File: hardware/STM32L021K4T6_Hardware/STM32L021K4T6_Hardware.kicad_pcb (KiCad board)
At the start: 2 copper layers, 60 x 50 mm, 27 parts, among them J1 Conn_02x07_Odd_Even, J2 INPUT, J3 POWER, J4 OUTPUT, U1 STM32L021K4Tx, U2 MCP1802x-xx02xOT, U3 MCP4801

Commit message: routage-ratnest
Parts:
- moved C10 22.9 mm to (105.0, 152.0), turned to -90 degrees
- moved C1 18.1 mm to (117.0, 149.0)
- moved R2 17.1 mm to (108.0, 136.0), turned to 90 degrees
- moved C2 15.9 mm to (102.0, 137.0)
- moved C3 15.7 mm to (102.0, 135.0)
- moved C6 15.6 mm to (102.0, 146.0), turned to -90 degrees
- moved C9 14.9 mm to (103.0, 151.9), turned to -90 degrees
- moved D1 6.96 mm to (120.0, 142.0), turned to 90 degrees
- moved J1 5.11 mm to (120.0, 133.7), turned to 180 degrees
- moved L1 5.00 mm to (102.0, 141.8), turned to -90 degrees
- moved R1 4.38 mm to (120.0, 146.0), turned to -90 degrees
- moved C4 4.23 mm to (100.0, 141.8)
- moved U3 3.27 mm to (110.5, 154.4)
- moved C5 3.00 mm to (100.0, 146.0), turned to -90 degrees
- moved D2 2.12 mm to (93.0, 131.1)
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
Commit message: sav_09_02_2024_22_45_drc_check
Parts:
- moved R1 76.2 mm to (167.0, 86.0), turned to 90 degrees
- moved J1 74.0 mm to (167.5, 77.1)
- moved U3 72.0 mm to (156.5, 98.9), turned to 180 degrees
- moved C1 71.8 mm to (162.0, 93.0), turned to -90 degrees
- moved L1 71.2 mm to (146.2, 86.0), turned to 0 degrees
- moved U1 71.1 mm to (155.0, 89.2)
- moved C10 71.1 mm to (150.0, 97.0)
- moved C2 71.1 mm to (147.0, 82.0)
- moved C3 71.1 mm to (147.0, 80.0)
- moved C7 71.1 mm to (149.0, 71.0)
- moved C8 71.1 mm to (141.0, 72.0)
- moved D2 71.1 mm to (138.0, 76.1)
- moved H1 71.1 mm to (130.0, 69.0)
- moved H2 71.1 mm to (180.0, 69.0)
- moved H3 71.1 mm to (180.0, 109.0)
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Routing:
- net NRST: track 0.00 -> 89.7 mm
- net +3.3V: track 0.00 -> 82.8 mm, vias 0 -> 2
- net USART2_RX: track 0.00 -> 39.5 mm, vias 0 -> 2
- net USART2_TX: track 0.00 -> 36.4 mm, vias 0 -> 2
- net DAC_OUT: track 0.00 -> 34.6 mm
- net +3.3VA: track 0.00 -> 29.5 mm
- net ADC_IN1: track 0.00 -> 24.5 mm, vias 0 -> 1
- net +5V: track 0.00 -> 12.3 mm
- net LED_STATUS: track 0.00 -> 12.1 mm
- net SWDCK: track 0.00 -> 11.2 mm
- net SWDIO: track 0.00 -> 11.1 mm
- net DAC_nCS: track 0.00 -> 9.23 mm
- net SPI1_SCK: track 0.00 -> 7.62 mm
- net SPI1_MOSI: track 0.00 -> 5.69 mm
- net GND: track 0.00 -> 4.78 mm
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
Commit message: drc_check_ok
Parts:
- moved C6 7.00 mm to (145.0, 89.0)
- moved C4 3.00 mm to (146.0, 92.0)
- moved C5 2.00 mm to (146.0, 94.0)
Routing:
- net NRST: track 89.7 -> 75.3 mm
- net +3.3VA: track 29.5 -> 30.1 mm

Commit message: drc check bis
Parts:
- moved C6 21.4 mm to (162.0, 76.0)
- moved L1 3.95 mm to (147.7, 89.7)
- moved D1 3.31 mm to (163.7, 89.7)
- moved R1 3.31 mm to (163.7, 85.8)
- moved J2 2.37 mm to (129.7, 88.7), turned to -90 degrees
- moved U3 1.91 mm to (155.1, 97.6)
- moved C4 1.75 mm to (147.7, 91.7)
- moved C5 1.75 mm to (147.7, 93.7)
- moved U2 0.99 mm to (146.0, 71.5)
- moved C7 0.99 mm to (149.9, 70.5)
- moved C8 0.99 mm to (141.9, 71.5)
- moved D2 0.99 mm to (138.9, 75.6)
- moved R3 0.99 mm to (138.9, 71.6)
- moved C1 0.76 mm to (161.3, 93.3)
- moved R2 0.70 mm to (153.0, 81.7)
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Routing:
- net NRST: track 75.3 -> 23.9 mm, vias 0 -> 2
- net +3.3V: track 82.8 -> 66.0 mm
- net +3.3VA: track 30.1 -> 19.9 mm
- net USART2_TX: track 36.4 -> 28.1 mm
- net LED_STATUS: track 12.1 -> 4.78 mm
- net GND: track 4.78 -> 9.15 mm, vias 0 -> 25
- net ADC_IN1: track 24.5 -> 27.5 mm
- net DAC_OUT: track 34.6 -> 32.3 mm
- net SPI1_MOSI: track 5.69 -> 3.56 mm
- net DAC_nLDAC: track 4.40 -> 2.52 mm
- net SPI1_SCK: track 7.62 -> 5.75 mm
- net DAC_nCS: track 9.23 -> 7.48 mm
- net SWDCK: track 11.2 -> 12.3 mm
- net +5V: track 12.3 -> 11.3 mm
- net SWDIO: track 11.1 -> 11.9 mm
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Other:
- board text added: "KARPUZ Ihsan - ENSEA 2024"

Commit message: drc check ok bis bis
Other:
- board text added: "KARPUZ Ihsan - CORNIL Josselin - ENSEA 2024"
- board text removed: "KARPUZ Ihsan - ENSEA 2024"

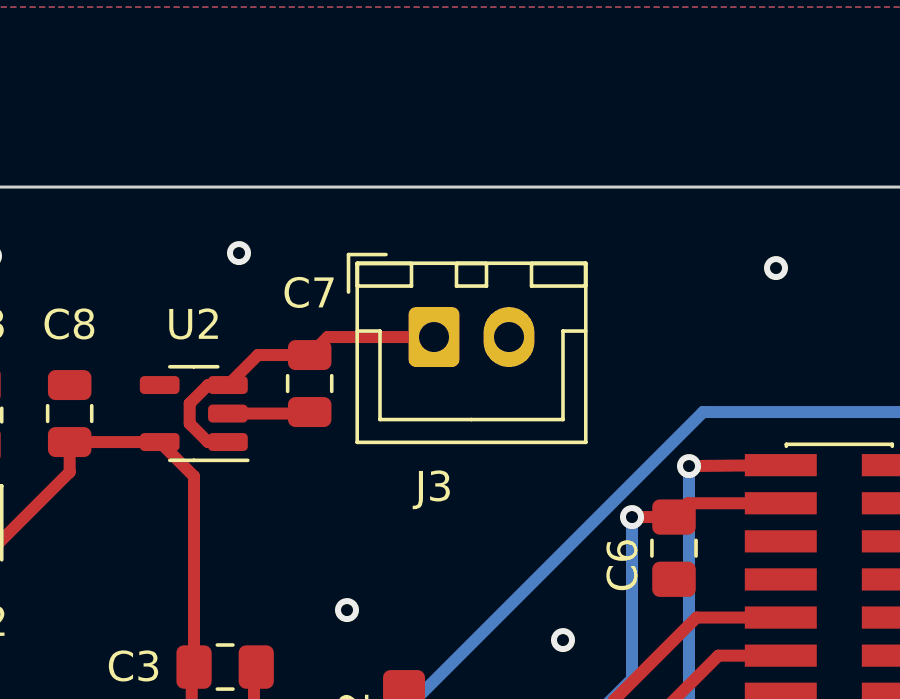
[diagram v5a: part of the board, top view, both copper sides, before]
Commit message: J3 reversed
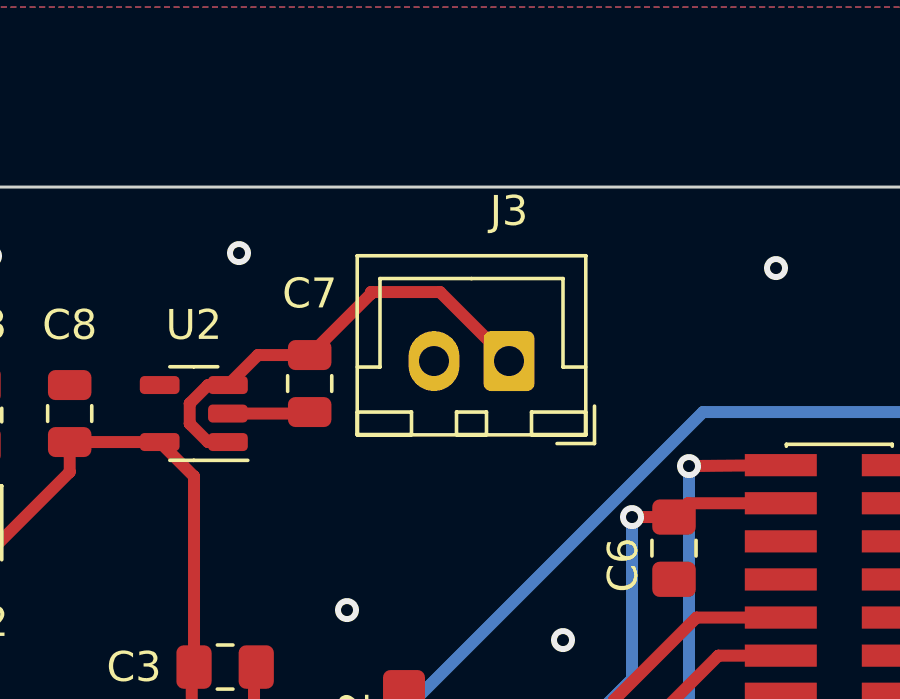
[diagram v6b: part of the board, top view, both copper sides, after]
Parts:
- moved J3 2.62 mm to (156.5, 69.8), turned to 180 degrees
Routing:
- net +5V: track 11.3 -> 15.4 mm
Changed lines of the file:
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@@
   )
   (footprint "Connector_JST:JST_XH_B2B-XH-A_1x02_P2.50mm_Vertical" (layer "F.Cu")
-    (at 154 69)
+    (at 156.5 69.8 180)
     (descr "JST XH series connector, B2B-XH-A (http://www.jst-mfg.com/product/pdf/eng/eXH.pdf), generated with kicad-footprint-generator")
     (tags "connector JST XH vertical")
@@
     (fp_line (start 4.95 3.4) (end 4.95 -2.35)
       (stroke (width 0.1) (type solid)) (layer "F.Fab"))
-    (pad "1" thru_hole roundrect (at 0 0) (size 1.7 2) (drill 1) (layers "*.Cu" "*.Mask") (roundrect_rratio 0.147059)
+    (pad "1" thru_hole roundrect (at 0 0 180) (size 1.7 2) (drill 1) (layers "*.Cu" "*.Mask") (roundrect_rratio 0.147059)
       (net 5 "+5V") (pinfunction "Pin_1") (pintype "passive"))
-    (pad "2" thru_hole oval (at 2.5 0) (size 1.7 2) (drill 1) (layers "*.Cu" "*.Mask")
+    (pad "2" thru_hole oval (at 2.5 0 180) (size 1.7 2) (drill 1) (layers "*.Cu" "*.Mask")
       (net 2 "GND") (pinfunction "Pin_2") (pintype "passive"))
     (model "${KICAD6_3DMODEL_DIR}/Connector_JST.3dshapes/JST_XH_B2B-XH-A_1x02_P2.50mm_Vertical.wrl"
@@
   (segment (start 148.131249 69.6) (end 147.131249 70.6) (width 0.4) (layer "F.Cu") (net 5))
   (segment (start 147.131249 70.6) (end 146.46875 70.6) (width 0.4) (layer "F.Cu") (net 5))
-  (segment (start 150.456249 69) (end 149.856249 69.6) (width 0.4) (layer "F.Cu") (net 5))
   (segment (start 146.46875 70.6) (end 145.856249 71.212501) (width 0.4) (layer "F.Cu") (net 5))
-  (segment (start 154 69) (end 150.456249 69) (width 0.4) (layer "F.Cu") (net 5))
+  (segment (start 149.856249 69.6) (end 151.9 67.556249) (width 0.4) (layer "F.Cu") (net 5))
+  (segment (start 151.9 67.5) (end 154.2 67.5) (width 0.4) (layer "F.Cu") (net 5))
   (segment (start 145.856249 71.887499) (end 146.46875 72.5) (width 0.4) (layer "F.Cu") (net 5))
+  (segment (start 151.9 67.556249) (end 151.9 67.5) (width 0.4) (layer "F.Cu") (net 5))
+  (segment (start 154.2 67.5) (end 156.5 69.8) (width 0.4) (layer "F.Cu") (net 5))
   (segment (start 145.856249 71.212501) (end 145.856249 71.887499) (width 0.4) (layer "F.Cu") (net 5))
   (segment (start 146.46875 72.5) (end 147.131249 72.5) (width 0.4) (layer "F.Cu") (net 5))
